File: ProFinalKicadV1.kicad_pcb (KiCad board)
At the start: 2 copper layers, 20 parts, among them SW501 SPST, U1 MICRO-B_USB, U2 MIC5219-3.3BM5, U3 FT231XS, U4 XB24-Z7WIT-004

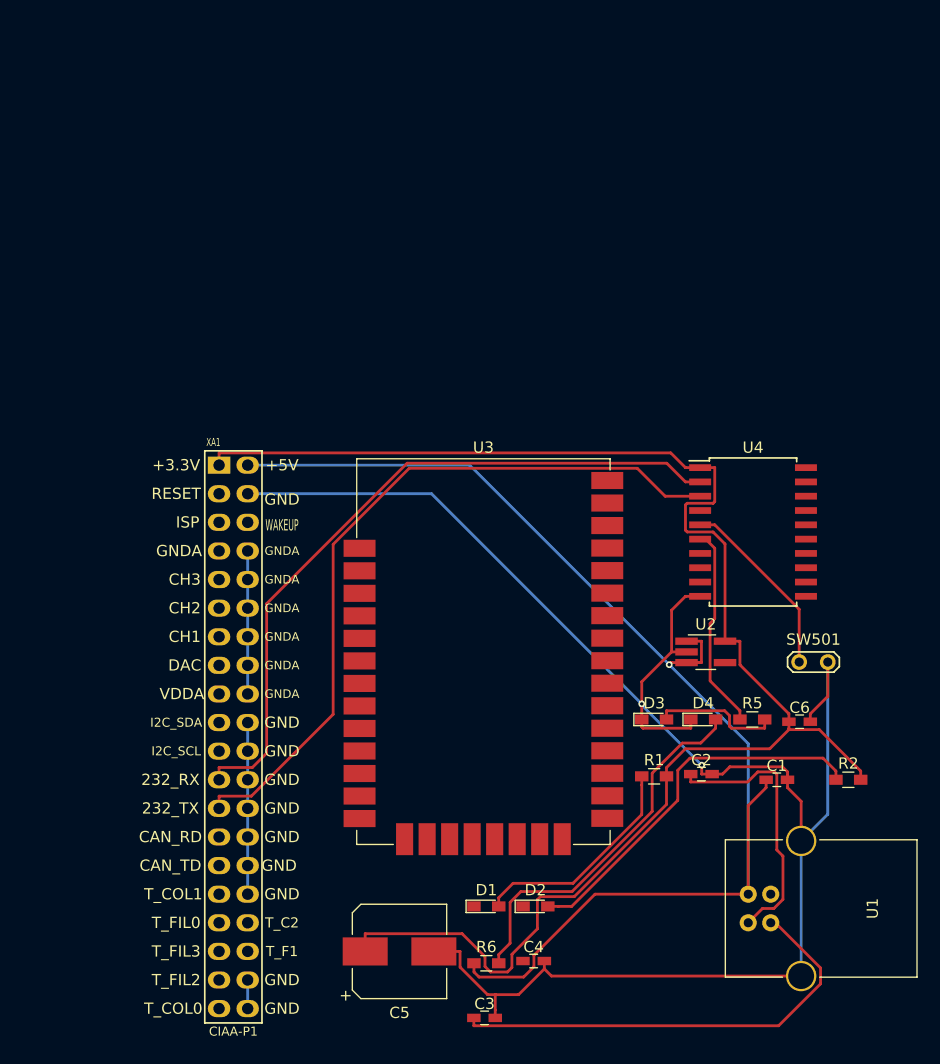
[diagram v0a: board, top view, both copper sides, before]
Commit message: Asociando 3D
3D de elementos previo a ruteo de PCB
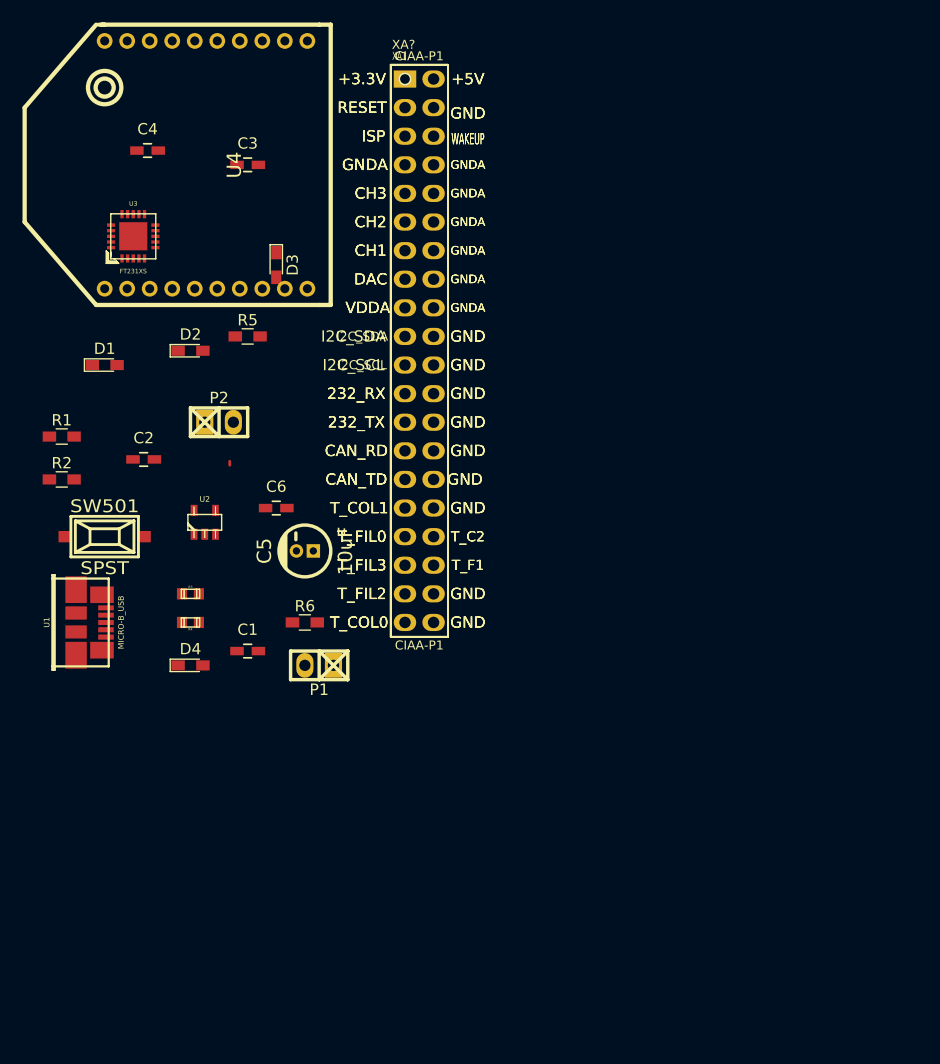
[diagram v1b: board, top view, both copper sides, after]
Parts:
- added P1: CONN_01X02, w_pin_strip.pretty:pin_socket_2, F.Cu at (156.2, 123.2)
- added P2: CONN_01X02, w_pin_strip.pretty:pin_socket_2, F.Cu at (147.3, 101.6)
- added R3: 27, R_27Ohm_pretty:r_0603, F.Cu at (144.8, 116.8)
- added R4: 27, R_27Ohm_pretty:r_0603, F.Cu at (144.8, 119.4)
- added XA?: Plantilla_Poncho_Derecha, CESE_pretty:Plantilla_Poncho_Derecha, F.Cu at (163.8, 71.1)
- C1, C4, C6: value C -> 0.1uF; footprint Capacitors_SMD:C_0603_HandSoldering -> C_0_1uF_pretty:C_0603_HandSoldering
- C2, C3: value C -> 47pF; footprint Capacitors_SMD:C_0603_HandSoldering -> C_47pF_pretty:C_0603_HandSoldering
- C5: value CP1 -> 10uF; footprint Capacitors_SMD:CP_Elec_8x10 -> C_10uF_pretty:CP_4x5mm
- D1, D3: value LED -> LED VERDE
- D2, D4: value LED -> LED ROJO
- R1, R2, R6: value R -> 1k
- R5: value R -> 330
- SW501: footprint Measurement_Points:Test_Point_2Pads -> Switch_pretty:smd_push
- U1: footprint Connect:USB_B -> USB_pretty:conn_usb_B_micro_smd
- U2: footprint TO_SOT_Packages_SMD:TSOT-23-5_HandSoldering -> MIC5219-3.3BM5_pretty:sot23-5
- U3: footprint RF_Modules:Digi_XBee_SMT -> FT231XS_pretty:qfn-20
- U4: footprint Housings_SOIC:SOIC-20W_7.5x12.8mm_Pitch1.27mm -> Xbee_pretty:XBee
- moved C4 79.7 mm to (141.0, 77.5)
- moved C3 78.6 mm to (149.9, 78.7)
- moved R2 74.8 mm to (133.3, 106.7)
- moved U4 66.2 mm to (137.2, 78.7), turned to 90 degrees
- moved U1 64.4 mm to (134.6, 119.4), turned to 270 degrees
- moved SW501 62.7 mm to (137.2, 111.8)
- moved R1 60.6 mm to (133.3, 102.9)
- moved D1 58.8 mm to (137.2, 96.5)
- moved D2 58.1 mm to (144.8, 95.2)
- moved C2 56.9 mm to (140.6, 104.9)
- moved R5 56.3 mm to (149.9, 94.0)
- moved D3 52.5 mm to (152.4, 87.6), turned to 270 degrees
- moved C6 50.2 mm to (152.4, 109.2)
- moved U3 48.8 mm to (139.7, 85.1)
- moved C1 48.4 mm to (149.9, 121.9)
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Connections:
- net /RSSI renamed Net-(R5-Pad1)
- C4 pad 1: Net-(C4-Pad1) -> (no net)
- D1 pad 1: Net-(D1-Pad1) -> (no net)
- D2 pad 1: Net-(D2-Pad1) -> (no net)
- SW501 pad 1: /RESET -> GND
- SW501 pad 2: GND -> Net-(SW501-Pad2)
- U1 pad 4: Net-(U1-Pad4) -> (no net)
- U2 pad 1: +5V -> Net-(P1-Pad2)
- U2 pad 4: Net-(U2-Pad4) -> (no net)
- U2 pad 5: +3V3 -> Net-(P2-Pad1)
- U4 pad 11: /DIO4 -> (no net)
- U4 pad 12: /CTS_XBEE -> (no net)
- U4 pad 13: /DIO9 -> (no net)
- U4 pad 14: /RES2 -> (no net)
- U4 pad 15: /DIO5 -> (no net)
- U4 pad 16: /RTS_XBEE -> (no net)
- U4 pad 17: /DIO3 -> (no net)
- U4 pad 18: /DIO2 -> (no net)
- U4 pad 19: /DIO1 -> (no net)
- U4 pad 20: /DIO0 -> (no net)
- U4 pad 4: /DIO12 -> (no net)
- U4 pad 5: /RESET -> Net-(SW501-Pad2)
- U4 pad 7: /DIO11 -> (no net)
- U4 pad 8: /RES1 -> (no net)
- U4 pad 9: /DTR_XBEE -> (no net)
- XA1 pad 11: Net-(XA1-Pad11) -> (no net)
- XA1 pad 13: Net-(XA1-Pad13) -> (no net)
- XA1 pad 15: Net-(XA1-Pad15) -> (no net)
- XA1 pad 17: Net-(XA1-Pad17) -> (no net)
- XA1 pad 19: Net-(XA1-Pad19) -> (no net)
- XA1 pad 21: Net-(XA1-Pad21) -> (no net)
- XA1 pad 27: Net-(XA1-Pad27) -> (no net)
- XA1 pad 29: Net-(XA1-Pad29) -> (no net)
- XA1 pad 3: Net-(XA1-Pad3) -> (no net)
- XA1 pad 31: Net-(XA1-Pad31) -> (no net)
- XA1 pad 33: Net-(XA1-Pad33) -> (no net)
- XA1 pad 34: Net-(XA1-Pad34) -> (no net)
- XA1 pad 35: Net-(XA1-Pad35) -> (no net)
- XA1 pad 36: Net-(XA1-Pad36) -> (no net)
- XA1 pad 37: Net-(XA1-Pad37) -> (no net)
- XA1 pad 39: Net-(XA1-Pad39) -> (no net)
- XA1 pad 5: Net-(XA1-Pad5) -> (no net)
- XA1 pad 6: Net-(XA1-Pad6) -> (no net)
- XA1 pad 7: Net-(XA1-Pad7) -> (no net)
- XA1 pad 9: Net-(XA1-Pad9) -> (no net)
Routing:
- net GND: track 160.7 -> 0.00 mm, vias 2 -> 0
- net +3V3: track 140.1 -> 0.00 mm
- net +5V: track 114.0 -> 0.00 mm, vias 1 -> 0
- net /DIN: track 65.7 -> 0.00 mm
- net /DOUT: track 63.5 -> 0.00 mm
- net /D+: track 40.5 -> 0.00 mm
- net Net-(D2-Pad2): track 33.9 -> 0.00 mm
- net Net-(D4-Pad2): track 33.3 -> 0.00 mm
- net /D-: track 24.1 -> 0.00 mm
- net Net-(D1-Pad2): track 19.9 -> 0.00 mm
- net Net-(R5-Pad1): track 18.1 -> 0.00 mm
- net /RESET: track 16.6 -> 0.00 mm
- net Net-(XA1-Pad20): track 15.2 -> 0.00 mm
- net Net-(XA1-Pad10): track 12.7 -> 0.00 mm
- net Net-(D3-Pad2): track 11.5 -> 0.00 mm
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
